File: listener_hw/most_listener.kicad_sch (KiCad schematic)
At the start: 111 parts, among them J1 1-1394640-1, J2 ANALYSER, J3 I2S, J4 VBAT_IN, J5 PLR135/T10, J6 PLT133/T10W, J7 RCA 75R, M1 Tang Nano 20K, M2 ESP32-DevKitC-VIE, U1 74LVC1G34, U10 TPS2553DBVR, U11 74LVC1G123, U12 DIR9001, U13 SRC4192, U14 LP5907MFX-3.3, U2 74LVC1G157, U3 74LVC1G125, U4 74LVC1G123, U5 TPS7B8133DRV, U6 LMR38020F, U7 Si514, U8 LP5907MFX-3.3, U9 74LVC1G79, X1 24.576MHz

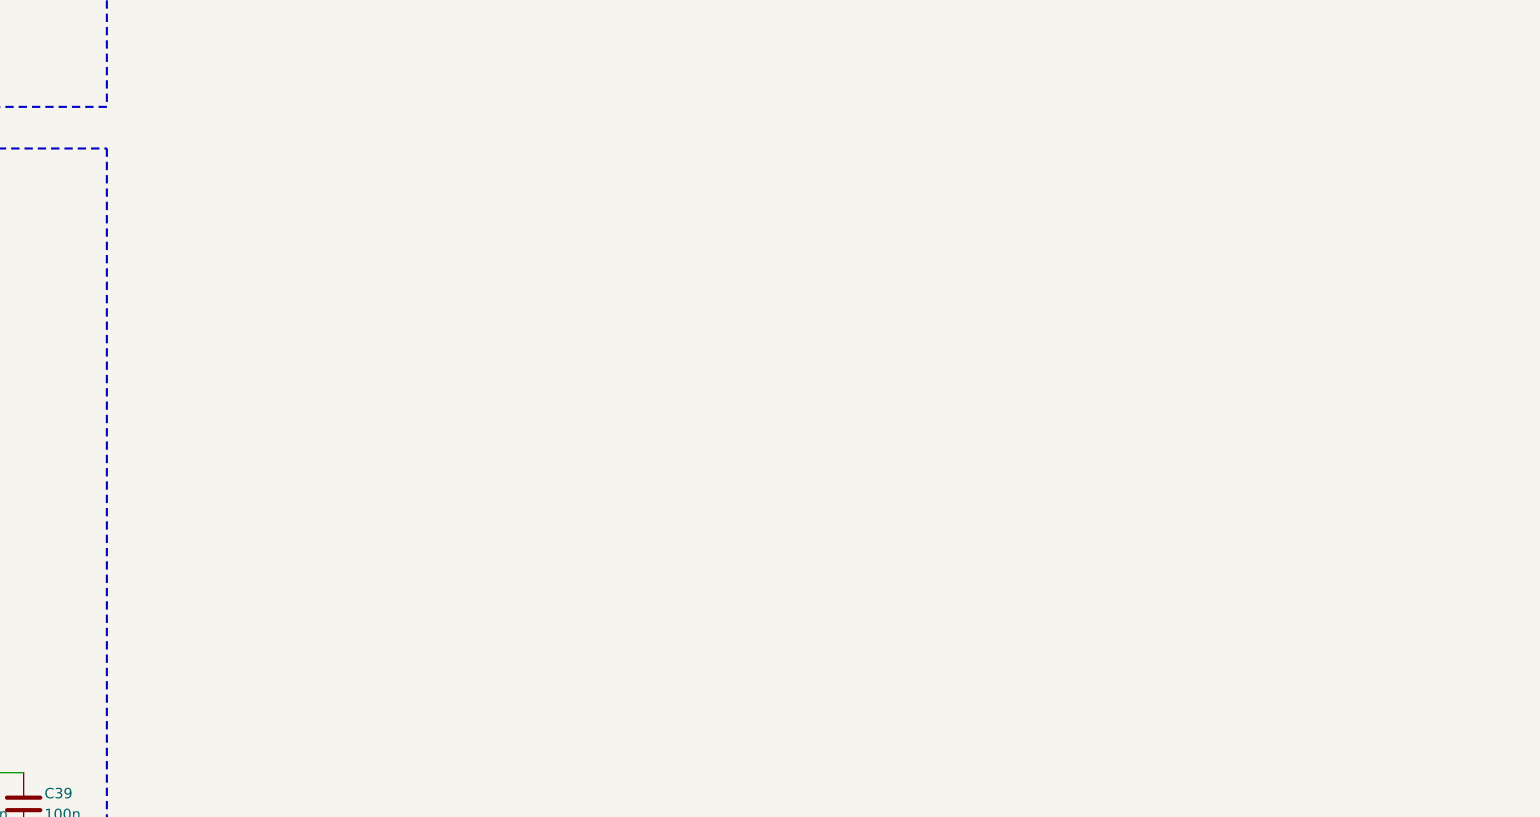
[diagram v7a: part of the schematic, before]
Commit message: Board: test points for the bench - RX_BUF, TX_REGEN, TX_SEL, WAKE, RT_CLK, the rails, GND
Block 10: 2 mm pads on the signals a scope must see in the bring-up order
(bypass, regeneration, injection) that are not on the module's header: the
FOT's line after U1, U9's retimed TX, U11's decision, the wake one-shot, the
Si514's clock at U9, 3V3_AON, 5V_SW and two grounds.

Co-Authored-By: Claude Fable 5.1 <noreply@anthropic.com>
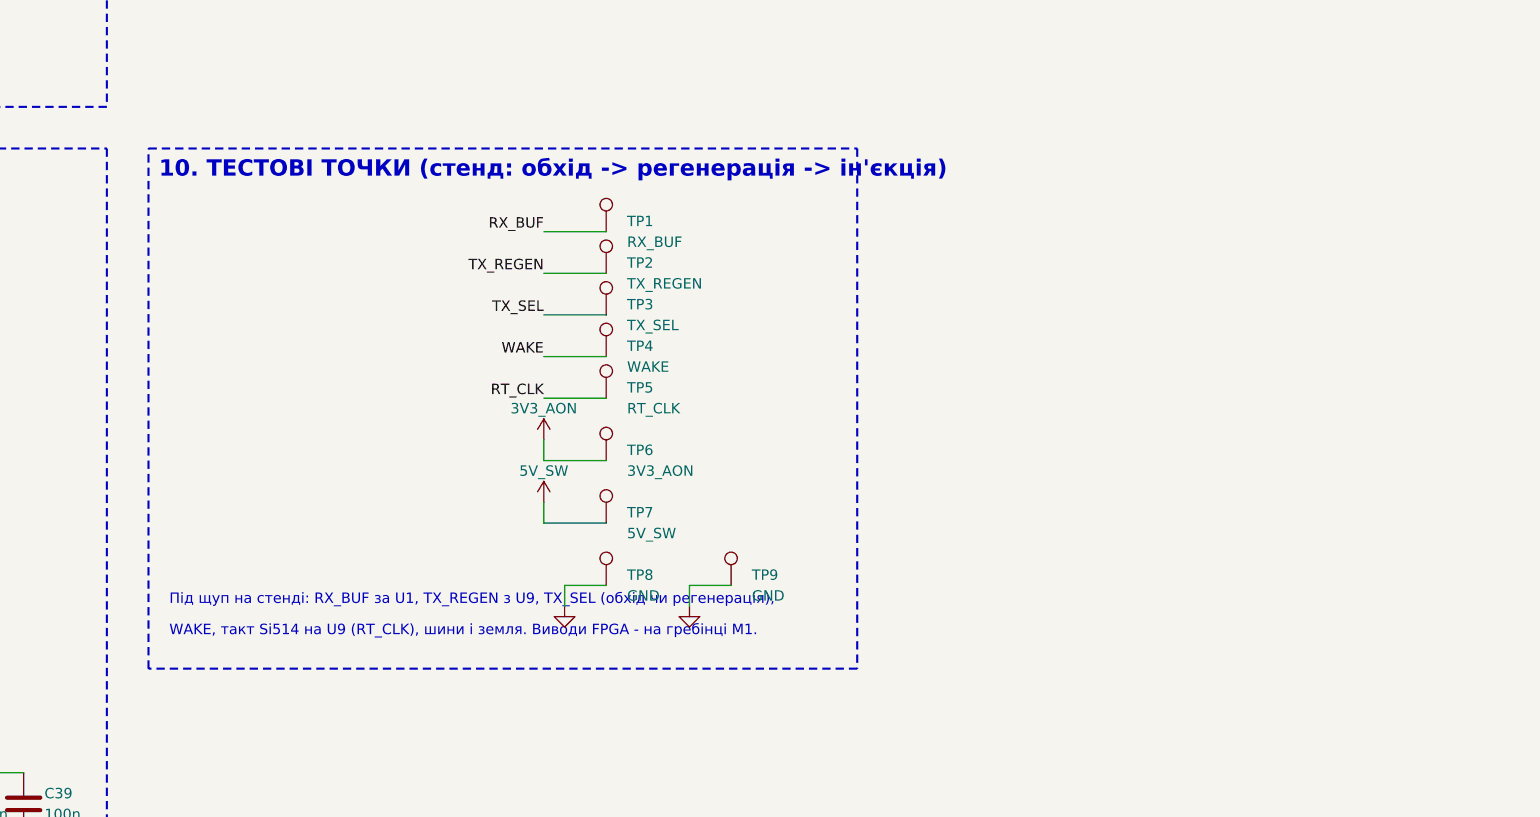
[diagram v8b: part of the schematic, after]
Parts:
- added TP1: RX_BUF, TestPoint:TestPoint_Pad_D2.0mm, symbol Connector:TestPoint
- added TP2: TX_REGEN, TestPoint:TestPoint_Pad_D2.0mm, symbol Connector:TestPoint
- added TP3: TX_SEL, TestPoint:TestPoint_Pad_D2.0mm, symbol Connector:TestPoint
- added TP4: WAKE, TestPoint:TestPoint_Pad_D2.0mm, symbol Connector:TestPoint
- added TP5: RT_CLK, TestPoint:TestPoint_Pad_D2.0mm, symbol Connector:TestPoint
- added TP6: 3V3_AON, TestPoint:TestPoint_Pad_D2.0mm, symbol Connector:TestPoint
- added TP7: 5V_SW, TestPoint:TestPoint_Pad_D2.0mm, symbol Connector:TestPoint
- added TP8, TP9: GND, TestPoint:TestPoint_Pad_D2.0mm, symbol Connector:TestPoint
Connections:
- net 3V3_AON: now also TP6.1
- net 5V_SW: now also TP7.1
- net GND: now also TP8.1, TP9.1
- net RT_CLK: now also TP5.1
- net RX_BUF: now also TP1.1
- net TX_REGEN: now also TP2.1
- net TX_SEL: now also TP3.1
- net WAKE: now also TP4.1
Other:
- note added: "10. ТЕСТОВІ ТОЧКИ (стенд: обхід -> регенерація -> ін'єкція)"
- note added: "WAKE, такт Si514 на U9 (RT_CLK), шини і земля. Виводи FPGA - на гребінці M1."
- note added: "Під щуп на стенді: RX_BUF за U1, TX_REGEN з U9, TX_SEL (обхід чи регенерація),"
